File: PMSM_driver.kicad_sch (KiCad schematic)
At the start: 56 parts, among them J1 22-23-2021, J2 302-S101, J3 Conn_01x03_Female, Q1 IRFH8334, Q2 IRFH8334, Q3 IRFH8334, Q4 IRFH8334, Q5 IRFH8334, Q6 IRFH8334, U1 IR2110, U2 IR2110, U3 IR2110, U4 LM358DT

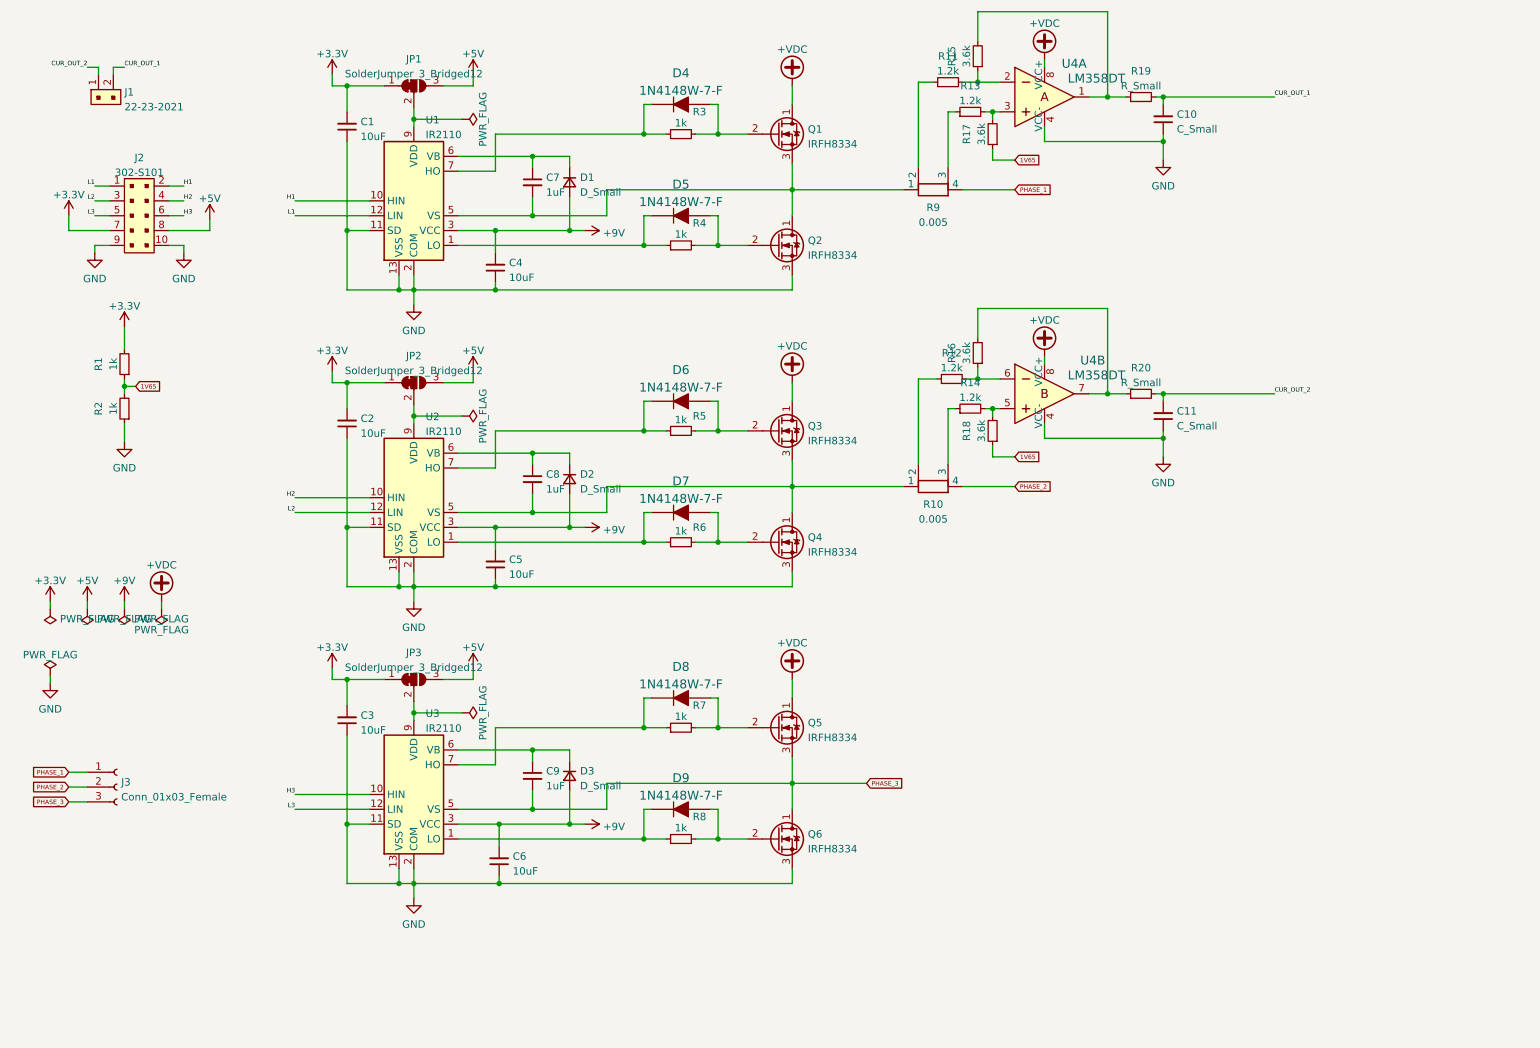
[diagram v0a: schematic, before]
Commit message: [sheme]: end of schematic + footprints assigment + bom
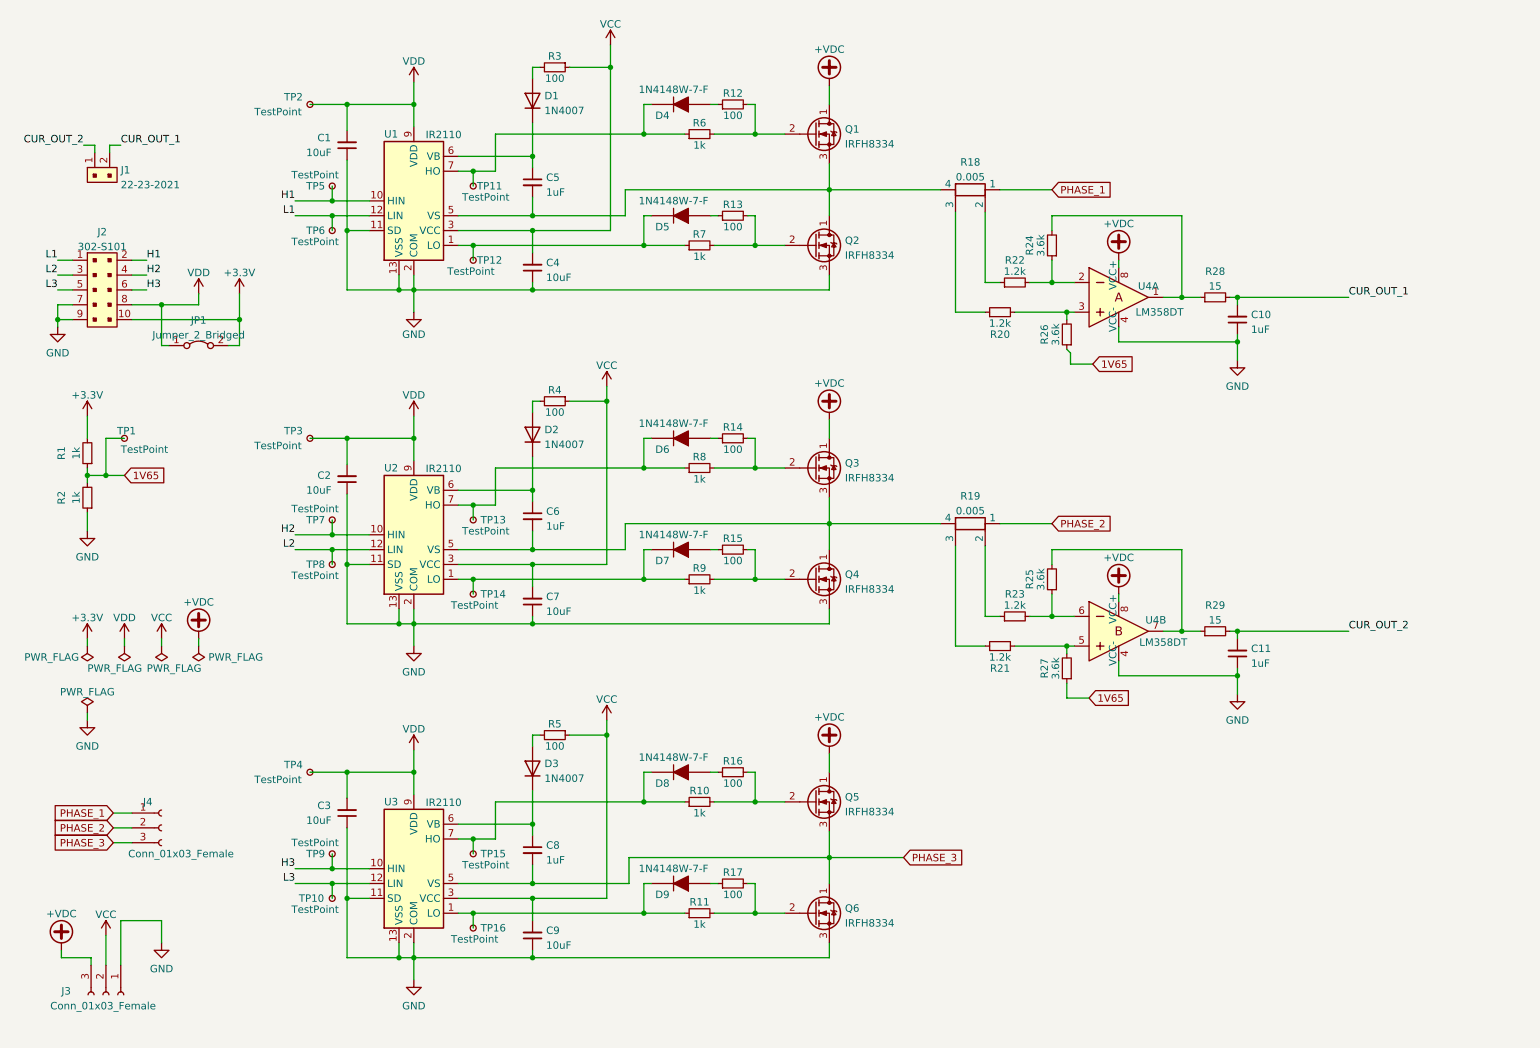
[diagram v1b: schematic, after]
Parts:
- removed D1, D2, D3: D_Small, symbol Device:D_Small
- removed JP1, JP2, JP3: SolderJumper_3_Bridged12, symbol Jumper:SolderJumper_3_Bridged12
- removed R6: 1k, symbol Device:R_Small
- added D1, D2, D3: 1N4007, Diode_THT:D_DO-41_SOD81_P10.16mm_Horizontal, symbol Diode:1N4007
- added J3: Conn_01x03_Female, Connector:Banana_Jack_3Pin, symbol Connector:Conn_01x03_Female
- added JP1: Jumper_2_Bridged, Jumper:SolderJumper-2_P1.3mm_Open_RoundedPad1.0x1.5mm, symbol Jumper:Jumper_2_Bridged
- added R10, R11, R9: 1k, Resistor_SMD:R_0603_1608Metric_Pad0.98x0.95mm_HandSolder, symbol Device:R_Small
- added R12, R13, R14, R15, R16, R17, R3: 100, Resistor_SMD:R_0603_1608Metric_Pad0.98x0.95mm_HandSolder, symbol Device:R_Small
- added TP1, TP10, TP11, TP12, TP13, TP14, TP15, TP16, TP2, TP3, TP4, TP5, TP6, TP7, TP8, TP9: TestPoint, TestPoint:TestPoint_Pad_D1.5mm, symbol Connector:TestPoint_Small
- C1, C2, C3, C4: footprint (none) -> Capacitor_SMD:C_1210_3225Metric_Pad1.33x2.70mm_HandSolder
- C10, C11: value C_Small -> 1uF; footprint (none) -> Capacitor_SMD:C_0805_2012Metric_Pad1.18x1.45mm_HandSolder
- C5: renamed from C7; footprint (none) -> Capacitor_SMD:C_0805_2012Metric_Pad1.18x1.45mm_HandSolder
- C6: renamed from C8; footprint (none) -> Capacitor_SMD:C_0805_2012Metric_Pad1.18x1.45mm_HandSolder
- C7: renamed from C5; footprint (none) -> Capacitor_SMD:C_1210_3225Metric_Pad1.33x2.70mm_HandSolder
- C8: renamed from C9; footprint (none) -> Capacitor_SMD:C_0805_2012Metric_Pad1.18x1.45mm_HandSolder
- C9: renamed from C6; footprint (none) -> Capacitor_SMD:C_1210_3225Metric_Pad1.33x2.70mm_HandSolder
- J4: renamed from J3; footprint (none) -> Connector:Banana_Jack_3Pin
- R1, R2, R7, R8: footprint (none) -> Resistor_SMD:R_0603_1608Metric_Pad0.98x0.95mm_HandSolder
- R18: renamed from R9; footprint Resistor_SMD:R_2512_6332Metric -> Resistor_SMD:R_2512_6332Metric_Pad1.40x3.35mm_HandSolder
- R19: renamed from R10; footprint Resistor_SMD:R_2512_6332Metric -> Resistor_SMD:R_2512_6332Metric_Pad1.40x3.35mm_HandSolder
- R20: renamed from R13; footprint (none) -> Resistor_SMD:R_0603_1608Metric_Pad0.98x0.95mm_HandSolder
- R21: renamed from R14; footprint (none) -> Resistor_SMD:R_0603_1608Metric_Pad0.98x0.95mm_HandSolder
- R22: renamed from R11; footprint (none) -> Resistor_SMD:R_0603_1608Metric_Pad0.98x0.95mm_HandSolder
- R23: renamed from R12; footprint (none) -> Resistor_SMD:R_0603_1608Metric_Pad0.98x0.95mm_HandSolder
- R24: renamed from R15; footprint (none) -> Resistor_SMD:R_0603_1608Metric_Pad0.98x0.95mm_HandSolder
- R25: renamed from R16; footprint (none) -> Resistor_SMD:R_0603_1608Metric_Pad0.98x0.95mm_HandSolder
- R26: renamed from R17; footprint (none) -> Resistor_SMD:R_0603_1608Metric_Pad0.98x0.95mm_HandSolder
- R27: renamed from R18; footprint (none) -> Resistor_SMD:R_0603_1608Metric_Pad0.98x0.95mm_HandSolder
- R28: renamed from R19; value R_Small -> 15; footprint (none) -> Resistor_SMD:R_0603_1608Metric_Pad0.98x0.95mm_HandSolder
- R29: renamed from R20; value R_Small -> 15; footprint (none) -> Resistor_SMD:R_0603_1608Metric_Pad0.98x0.95mm_HandSolder
- R4, R5: value 1k -> 100; footprint (none) -> Resistor_SMD:R_0603_1608Metric_Pad0.98x0.95mm_HandSolder
- R6: renamed from R3; footprint (none) -> Resistor_SMD:R_0603_1608Metric_Pad0.98x0.95mm_HandSolder
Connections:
- net +5V is gone; now on net VDD: J2.8
- net +3.3V: now also J2.10, JP1.2 (B); no longer C1.2, C2.2, C3.2, J2.7
- net +VDC: now also J3.3 (Pin_3)
- net 1V65: now also TP1.1
- net GND: now also J2.7, J3.1 (Pin_1); no longer J2.10
- net H1: now also TP5.1
- net H2: now also TP7.1
- net H3: now also TP9.1
- net L1: now also TP6.1
- net L2: now also TP8.1
- net L3: now also TP10.1
- net PHASE_1: now also R18.1; no longer R18.4
- net PHASE_2: now also R19.1; no longer R19.4
- net at Q4.2 (G): now also R15.2, R9.2; no longer D7.A
- net at D7.K, U2.1 (LO): now also R9.1, TP14.1
- net at D8.K, U3.7 (HO): now also R10.1, TP15.1; no longer R7.1
- net at D6.K, U2.7 (HO): now also R8.1, TP13.1; no longer R5.1
- net at D5.K, U1.1 (LO): now also R7.1, TP12.1; no longer R4.1
- net VDD: now reaches U2.9 (VDD)
- net VDD: now also C1.2, C2.2, C3.2, U1.9 (VDD), U3.9 (VDD), JP1.1 (A), TP2.1, TP3.1, TP4.1
- net at D9.K, U3.1 (LO): now also R11.1, TP16.1; no longer R8.1
- net at D4.K, R6.1, U1.7 (HO): now also TP11.1
- net at Q1.2 (G), R6.2: now also R12.2; no longer D4.A
- net at C5.1, U1.6 (VB): now also D1.1 (K)
- net at C5.2, Q1.3 (S), Q2.1 (D)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: now also R18.4; no longer R18.1
- net at C6.2, Q3.3 (S), Q4.1 (D)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: now also R19.4; no longer R19.1
- net at C8.1, U3.6 (VB): now also D3.1 (K)
- net at C6.1, U2.6 (VB): now also D2.1 (K)
- net +9V renamed VCC
- net VCC: now also R4.1, R5.1, J3.2 (Pin_2), R3.1
- new net: D3.2 (A), R5.2
- new net: D7.A, R15.1
- new net: Q5.2 (G), R10.2, R16.2
- new net: D2.2 (A), R4.2
- new net: D1.2 (A), R3.2
- new net: Q6.2 (G), R11.2, R17.2
- new net: D5.A, R13.1
- new net: D6.A, R14.1
- new net: Q3.2 (G), R14.2, R8.2
- new net: D4.A, R12.1
- new net: D9.A, R17.1
- new net: Q2.2 (G), R13.2, R7.2
- new net: D8.A, R16.1
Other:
- moved on the sheet: C1, C10, C11, C2, C3, C4, C6, C7, C8, C9, J1, J2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

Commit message: [PCB]: PCB design started. Schematic updated.
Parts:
- removed J3: Conn_01x03_Female, Connector:Banana_Jack_3Pin, symbol Connector:Conn_01x03_Female
- removed R18, R19: 0.005, Resistor_SMD:R_2512_6332Metric_Pad1.40x3.35mm_HandSolder, symbol Device:R_Shunt
- added J3: Conn_Bridge_Power, Connector:Banana_Jack_2Pin, symbol Connector:Conn_01x02_Female
- added J5: Conn_Driver_Power, Connector:Banana_Jack_2Pin, symbol Connector:Conn_01x02_Female
- added R18, R19: 0.005, Resistor_SMD:R_2512_6332Metric_Pad1.40x3.35mm_HandSolder, symbol Device:R_Small
- J4: value Conn_01x03_Female -> Conn_Phases
- renumbered C5 to C4, C4 to C5
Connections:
- net +VDC: now also Q1.5 (D), Q1.6 (D), Q1.7 (D), Q1.8 (D), Q3.5 (D), Q3.6 (D), Q3.7 (D), Q3.8 (D), Q5.5 (D), Q5.6 (D), Q5.7 (D), Q5.8 (D), J3.1 (Pin_1); no longer Q1.1 (D), Q3.1 (D), Q5.1 (D)
- net GND: now also Q2.1 (S), Q2.2 (S), Q4.1 (S), Q4.2 (S), Q6.1 (S), Q6.2 (S), J3.2 (Pin_2), J5.2 (Pin_2)
- net PHASE_1: now also R22.1, R18.1
- net PHASE_2: now also R23.1, R19.1
- net PHASE_3: now also Q5.1 (S), Q5.2 (S), Q6.5 (D), Q6.6 (D), Q6.7 (D), Q6.8 (D); no longer Q6.1 (D)
- net VCC: now also J5.1 (Pin_1)
- net at R15.2, R9.2: now also Q4.4 (G); no longer Q4.2 (G)
- net at R10.2, R16.2: now also Q5.4 (G); no longer Q5.2 (G)
- net at R11.2, R17.2: now also Q6.4 (G); no longer Q6.2 (G)
- net at R21.1: now also C6.2, Q3.1 (S), Q3.2 (S), Q3.3 (S), Q4.5 (D), Q4.6 (D), Q4.7 (D), Q4.8 (D), U2.5 (VS), R19.2
- net at R12.2, R6.2: now also Q1.4 (G); no longer Q1.2 (G)
- net at C4.2, Q1.3 (S), U1.5 (VS): now also Q1.1 (S), Q1.2 (S), Q2.5 (D), Q2.6 (D), Q2.7 (D), Q2.8 (D), R20.1, R18.2; no longer Q2.1 (D)
- net at R14.2, R8.2: now also Q3.4 (G); no longer Q3.2 (G)
- net at R13.2, R7.2: now also Q2.4 (G); no longer Q2.2 (G)

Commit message: [PCB]: components arrangment around 3 MOSFET drivers
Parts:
- removed J3: Conn_Bridge_Power, Connector:Banana_Jack_2Pin, symbol Connector:Conn_01x02_Female
- removed J5: Conn_Driver_Power, Connector:Banana_Jack_2Pin, symbol Connector:Conn_01x02_Female
- removed TP2, TP3, TP4: TestPoint, TestPoint:TestPoint_Pad_D1.5mm, symbol Connector:TestPoint_Small
- added J3: Screw_Terminal_Power, TerminalBlock_Phoenix:TerminalBlock_Phoenix_MKDS-1,5-2_1x02_P5.00mm_Horizontal, symbol Connector:Screw_Terminal_01x02
- added J5: Screw_Terminal_Logic, TerminalBlock_Phoenix:TerminalBlock_Phoenix_MKDS-1,5-2_1x02_P5.00mm_Horizontal, symbol Connector:Screw_Terminal_01x02
- J2: footprint digikey-footprints:PinHeader_2x5_P2.54mm_Drill1.2mm -> Connector_PinHeader_2.54mm:PinHeader_2x05_P2.54mm_Vertical
- renumbered TP13 to TP10, TP14 to TP11, TP15 to TP12, TP16 to TP13, TP5 to TP2, TP6 to TP3, TP7 to TP4, TP8 to TP5, TP9 to TP6, TP10 to TP7, TP11 to TP8, TP12 to TP9
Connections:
- net +VDC: now also J3.1 (Pin_1)
- net GND: now also J3.2 (Pin_2), J5.2 (Pin_2)
- net VCC: now also J5.1 (Pin_1)

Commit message: [PCB]: added Power part of the board. Logic part rearrangement
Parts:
- removed J4: Conn_Phases, Connector:Banana_Jack_3Pin, symbol Connector:Conn_01x03_Female
- added J3: Screw_Terminal_1, TestPoint:TestPoint_Pad_4.0x4.0mm, symbol Connector:Screw_Terminal_01x01
- added J4: Screw_Terminal_2, TestPoint:TestPoint_Pad_4.0x4.0mm, symbol Connector:Screw_Terminal_01x01
- added J5: Screw_Terminal_3, TestPoint:TestPoint_Pad_4.0x4.0mm, symbol Connector:Screw_Terminal_01x01
- J1: footprint digikey-footprints:PinHeader_1x2_P2.54mm_Drill1.02mm -> Connector_PinHeader_2.54mm:PinHeader_1x02_P2.54mm_Vertical
- renumbered J3 to J2, J5 to J6, J2 to J7
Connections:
- net +3.3V: now also J7.7; no longer J7.10
- net GND: now also J7.5, J7.6; no longer J7.7, J7.9
- net H1: now also J7.1; no longer J7.2
- net H3: now also J7.10; no longer J7.6
- net L1: now also J7.2; no longer J7.1
- net L2: now also J7.8; no longer J7.3
- net L3: now also J7.9; no longer J7.5
- net PHASE_1: now also J3.1 (Pin_1)
- net PHASE_2: now also J4.1 (Pin_1)
- net PHASE_3: now also J5.1 (Pin_1)
- net VDD: now also J7.3; no longer J7.8
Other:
- moved on the sheet: J7, JP1

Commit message: [PCB]: size optimization
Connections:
- net Q1_Q2: now reaches C4.2, Q1.1 (S), Q1.2 (S), Q1.3 (S), Q2.5 (D), Q2.6 (D), Q2.7 (D), Q2.8 (D), R18.2, R20.1, U1.5 (VS)
- net Q3_Q4: now reaches C6.2, Q3.1 (S), Q3.2 (S), Q3.3 (S), Q4.5 (D), Q4.6 (D), Q4.7 (D), Q4.8 (D), R19.2, R21.1, U2.5 (VS)
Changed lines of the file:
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@@
     (effects (font (size 1.27 1.27)) (justify right bottom))
+  )
+  (label "Q5_Q6" (at 152.4 160.528 0)
+    (effects (font (size 1.27 1.27)) (justify left bottom))
   )
   (label "CUR_OUT_1" (at 31.115 38.735 0)
@@
     (effects (font (size 1.27 1.27)) (justify right bottom))
   )
+  (label "Q1_Q2" (at 152.4 46.228 0)
+    (effects (font (size 1.27 1.27)) (justify left bottom))
+  )
   (label "L1" (at 50.8 59.69 0)
     (effects (font (size 1.27 1.27)) (justify left bottom))
@@
     (effects (font (size 1.27 1.27)) (justify right bottom))
   )
+  (label "Q3_Q4" (at 152.4 103.378 0)
+    (effects (font (size 1.27 1.27)) (justify left bottom))
+  )
   (global_label "PHASE_3" (shape input) (at 165.1 160.655 0) (fields_autoplaced)

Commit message: [PCB]: Logic - Power boards tracing
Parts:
- added J10: Conn21, Connector_PinHeader_2.54mm:PinHeader_2x02_P2.54mm_Vertical, symbol Connector_Generic:Conn_02x02_Odd_Even
- added J11: Conn22, Connector_PinHeader_2.54mm:PinHeader_2x02_P2.54mm_Vertical, symbol Connector_Generic:Conn_02x02_Odd_Even
- added J12: Conn31, Connector_PinHeader_2.54mm:PinHeader_2x02_P2.54mm_Vertical, symbol Connector_Generic:Conn_02x02_Odd_Even
- added J13: Conn32, Connector_PinHeader_2.54mm:PinHeader_2x02_P2.54mm_Vertical, symbol Connector_Generic:Conn_02x02_Odd_Even
- added J8: Conn11, Connector_PinHeader_2.54mm:PinHeader_2x02_P2.54mm_Vertical, symbol Connector_Generic:Conn_02x02_Odd_Even
- added J9: Conn12, Connector_PinHeader_2.54mm:PinHeader_2x02_P2.54mm_Vertical, symbol Connector_Generic:Conn_02x02_Odd_Even
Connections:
- net GND: now also J10.1 (Pin_1), J11.1 (Pin_1), J12.2 (Pin_2), J13.2 (Pin_2), J8.3 (Pin_3), J9.3 (Pin_3)
- net PHASE_3: now also J12.1 (Pin_1), J13.1 (Pin_1)
- net Q1_Q2: now also J8.4 (Pin_4), J9.4 (Pin_4)
- net Q3_Q4: now also J10.2 (Pin_2), J11.2 (Pin_2)
- net Q4_G: now reaches Q4.4 (G), R15.2, R9.2
- net Q4_G: now also J10.3 (Pin_3), J11.3 (Pin_3)
- net Q5_G: now reaches Q5.4 (G), R10.2, R16.2
- net Q5_G: now also J12.3 (Pin_3), J13.3 (Pin_3)
- net Q6_G: now reaches Q6.4 (G), R11.2, R17.2
- net Q6_G: now also J12.4 (Pin_4), J13.4 (Pin_4)
- net Q1_G: now reaches Q1.4 (G), R12.2, R6.2
- net Q1_G: now also J8.2 (Pin_2), J9.2 (Pin_2)
- net Q3_G: now reaches Q3.4 (G), R14.2, R8.2
- net Q3_G: now also J10.4 (Pin_4), J11.4 (Pin_4)
- net Q2_G: now reaches Q2.4 (G), R13.2, R7.2
- net Q2_G: now also J8.1 (Pin_1), J9.1 (Pin_1)

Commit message: [DRC]: DRC checks were passed
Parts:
- removed J1: 22-23-2021, Connector_PinHeader_2.54mm:PinHeader_1x02_P2.54mm_Vertical, symbol dk_Rectangular-Connectors-Headers-Male-Pins:22-23-2021
- removed TP2, TP3, TP4, TP5, TP6, TP7: TestPoint, TestPoint:TestPoint_Pad_D1.5mm, symbol Connector:TestPoint_Small
- added J1: 640456-3, Connector_PinHeader_2.54mm:PinHeader_1x03_P2.54mm_Vertical, symbol dk_Rectangular-Connectors-Headers-Male-Pins:640456-3
- renumbered TP8 to TP2, TP9 to TP3, TP10 to TP4, TP11 to TP5, TP12 to TP6, TP13 to TP7
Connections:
- net +3.3V: now also J1.3
- net CUR_OUT_1: now also J1.1
- net CUR_OUT_2: now also J1.2
- net Q3_G: now also J10.3 (Pin_3), J11.3 (Pin_3); no longer J10.4 (Pin_4), J11.4 (Pin_4)
- net Q4_G: now also J10.4 (Pin_4), J11.4 (Pin_4); no longer J10.3 (Pin_3), J11.3 (Pin_3)
